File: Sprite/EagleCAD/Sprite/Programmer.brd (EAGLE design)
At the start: 49.5 x 49.5 mm, 5 parts

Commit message: Programmer Board
Finished programmer shield board
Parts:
- added JP5: (no value), SparkFun:1X03_LOCK
- moved JP3 10.2 mm to (3.81, 45.1), turned to 270 degrees
- moved JP2 5.68 mm to (32.0, 37.6), turned to 0 degrees
- moved JP1 2.57 mm to (37.1, 40.2)
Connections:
- new net 3.3V: JP2.1, JP3.1
- new net RST: JP2.2, JP3.3
- new net RXD: JP2.3, JP4.1
- new net TEST: JP1.2, JP3.2
- new net TXD: JP1.1, JP3.4
- net GND: now also JP1.3, JP5.1, JP5.2
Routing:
- net TXD: track 0.00 -> 55.0 mm
- net RST: track 0.00 -> 47.3 mm
- net TEST: track 0.00 -> 43.6 mm
- net 3.3V: track 0.00 -> 34.2 mm
- net RXD: track 0.00 -> 33.1 mm
- net GND: track 0.00 -> 16.3 mm
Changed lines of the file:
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@@
 <elements>
 <element name="U$1" library="TI_launchpad" package="LAUNCHPAD-50MM" value="LAUNCHPAD-50MM" x="0" y="-0.635"/>
-<element name="JP1" library="SparkFun" package="1X03_LOCK" value="" x="37.1" y="37.6" rot="R180"/>
-<element name="JP2" library="SparkFun" package="1X03_LOCK" value="" x="37.1" y="40.14" rot="R180"/>
-<element name="JP3" library="SparkFun" package="1X05_LOCK" value="" x="3.81" y="34.925" rot="R90"/>
+<element name="JP1" library="SparkFun" package="1X03_LOCK" value="" x="37.1" y="40.1654" rot="R180"/>
+<element name="JP2" library="SparkFun" package="1X03_LOCK" value="" x="32.0134" y="37.6094"/>
+<element name="JP3" library="SparkFun" package="1X05_LOCK" value="" x="3.81" y="45.085" rot="R270"/>
 <element name="JP4" library="SparkFun" package="1X05_LOCK" value="" x="6.35" y="34.925" rot="R90"/>
+<element name="JP5" library="SparkFun" package="1X03_LOCK" value="" x="41.91" y="47.625"/>
 </elements>
 <signals>
@@
 <signal name="GND">
 <contactref element="U$1" pad="GND"/>
+<contactref element="JP1" pad="3"/>
+<wire x1="40.5638" y1="47.752" x2="37.0332" y2="44.2214" width="0.4064" layer="16"/>
+<wire x1="37.0332" y1="44.2214" x2="33.0708" y2="44.2214" width="0.4064" layer="16"/>
+<wire x1="33.0708" y1="44.2214" x2="32.004" y2="43.1546" width="0.4064" layer="16"/>
+<wire x1="32.004" y1="43.1546" x2="32.004" y2="40.0544" width="0.4064" layer="16"/>
+<wire x1="32.004" y1="40.0544" x2="32.02" y2="40.0384" width="0.4064" layer="16"/>
+<contactref element="JP5" pad="2"/>
+<contactref element="JP5" pad="1"/>
+<wire x1="44.45" y1="47.498" x2="42.0878" y2="47.498" width="0.4064" layer="16"/>
+<wire x1="42.0878" y1="47.498" x2="41.8338" y2="47.752" width="0.4064" layer="16"/>
+<wire x1="41.8338" y1="47.752" x2="41.91" y2="47.752" width="0" layer="19" extent="16-16"/>
+<wire x1="40.5638" y1="47.752" x2="41.8338" y2="47.752" width="0" layer="19" extent="16-16"/>
+<wire x1="13.97" y1="47.625" x2="32.004" y2="43.1546" width="0" layer="19" extent="16-16"/>
+</signal>
+<signal name="3.3V">
+<contactref element="JP2" pad="1"/>
+<wire x1="32.004" y1="37.727" x2="32.0134" y2="37.7364" width="0.4064" layer="16"/>
+<contactref element="JP3" pad="1"/>
+<wire x1="32.004" y1="37.727" x2="19.8548" y2="37.727" width="0.4064" layer="16"/>
+<wire x1="19.8548" y1="37.727" x2="10.0584" y2="47.5234" width="0.4064" layer="16"/>
+<wire x1="10.0584" y1="47.5234" x2="4.6228" y2="47.5234" width="0.4064" layer="16"/>
+<wire x1="4.6228" y1="47.5234" x2="3.9116" y2="46.8122" width="0.4064" layer="16"/>
+<wire x1="3.9116" y1="46.8122" x2="3.9116" y2="45.1104" width="0.4064" layer="16"/>
+<wire x1="3.9116" y1="45.1104" x2="3.937" y2="45.085" width="0.4064" layer="16"/>
+</signal>
+<signal name="RST">
+<contactref element="JP2" pad="2"/>
+<contactref element="JP3" pad="3"/>
+<wire x1="34.5534" y1="37.4824" x2="34.5534" y2="34.147" width="0.4064" layer="1"/>
+<wire x1="34.5534" y1="34.147" x2="32.131" y2="31.7246" width="0.4064" layer="1"/>
+<wire x1="32.131" y1="31.7246" x2="3.1242" y2="31.7246" width="0.4064" layer="1"/>
+<wire x1="3.1242" y1="31.7246" x2="1.2446" y2="33.6042" width="0.4064" layer="1"/>
+<wire x1="1.2446" y1="33.6042" x2="1.2446" y2="39.5478" width="0.4064" layer="1"/>
+<wire x1="1.2446" y1="39.5478" x2="1.7272" y2="40.0304" width="0.4064" layer="1"/>
+<wire x1="1.7272" y1="40.0304" x2="3.9116" y2="40.0304" width="0.4064" layer="1"/>
+<wire x1="3.9116" y1="40.0304" x2="3.937" y2="40.005" width="0.4064" layer="1"/>
+</signal>
+<signal name="TEST">
+<contactref element="JP1" pad="2"/>
+<contactref element="JP3" pad="2"/>
+<wire x1="34.56" y1="40.2924" x2="34.56" y2="41.4114" width="0.4064" layer="1"/>
+<wire x1="34.56" y1="41.4114" x2="31.75" y2="44.2214" width="0.4064" layer="1"/>
+<wire x1="31.75" y1="44.2214" x2="11.8364" y2="44.2214" width="0.4064" layer="1"/>
+<wire x1="11.8364" y1="44.2214" x2="8.2296" y2="47.8282" width="0.4064" layer="1"/>
+<wire x1="8.2296" y1="47.8282" x2="2.4384" y2="47.8282" width="0.4064" layer="1"/>
+<wire x1="2.4384" y1="47.8282" x2="1.397" y2="46.7868" width="0.4064" layer="1"/>
+<wire x1="1.397" y1="46.7868" x2="1.397" y2="43.1292" width="0.4064" layer="1"/>
+<wire x1="1.397" y1="43.1292" x2="1.9304" y2="42.5958" width="0.4064" layer="1"/>
+<wire x1="1.9304" y1="42.5958" x2="3.6322" y2="42.5958" width="0.4064" layer="1"/>
+<wire x1="3.6322" y1="42.5958" x2="3.683" y2="42.545" width="0.4064" layer="1"/>
+</signal>
+<signal name="TXD">
+<contactref element="JP3" pad="4"/>
+<contactref element="JP1" pad="1"/>
+<wire x1="37.1" y1="40.0384" x2="39.1334" y2="40.0384" width="0.4064" layer="16"/>
+<wire x1="39.1334" y1="40.0384" x2="40.4114" y2="38.7604" width="0.4064" layer="16"/>
+<wire x1="40.4114" y1="38.7604" x2="40.4114" y2="32.9946" width="0.4064" layer="16"/>
+<wire x1="40.4114" y1="32.9946" x2="39.7764" y2="32.3596" width="0.4064" layer="16"/>
+<wire x1="39.7764" y1="32.3596" x2="2.8194" y2="32.3596" width="0.4064" layer="16"/>
+<wire x1="2.8194" y1="32.3596" x2="1.4478" y2="33.7312" width="0.4064" layer="16"/>
+<wire x1="1.4478" y1="33.7312" x2="1.4478" y2="36.83" width="0.4064" layer="16"/>
+<wire x1="1.4478" y1="36.83" x2="2.0574" y2="37.4396" width="0.4064" layer="16"/>
+<wire x1="2.0574" y1="37.4396" x2="3.6576" y2="37.4396" width="0.4064" layer="16"/>
+<wire x1="3.6576" y1="37.4396" x2="3.683" y2="37.465" width="0.4064" layer="16"/>
+</signal>
+<signal name="RXD">
+<contactref element="JP4" pad="1"/>
+<contactref element="JP2" pad="3"/>
+<wire x1="37.0934" y1="37.7364" x2="37.0934" y2="35.925" width="0.4064" layer="16"/>
+<wire x1="37.0934" y1="35.925" x2="36.068" y2="34.8996" width="0.4064" layer="16"/>
+<wire x1="36.068" y1="34.8996" x2="6.2484" y2="34.8996" width="0.4064" layer="16"/>
+<wire x1="6.2484" y1="34.8996" x2="6.223" y2="34.925" width="0.4064" layer="16"/>
 </signal>
 </signals>

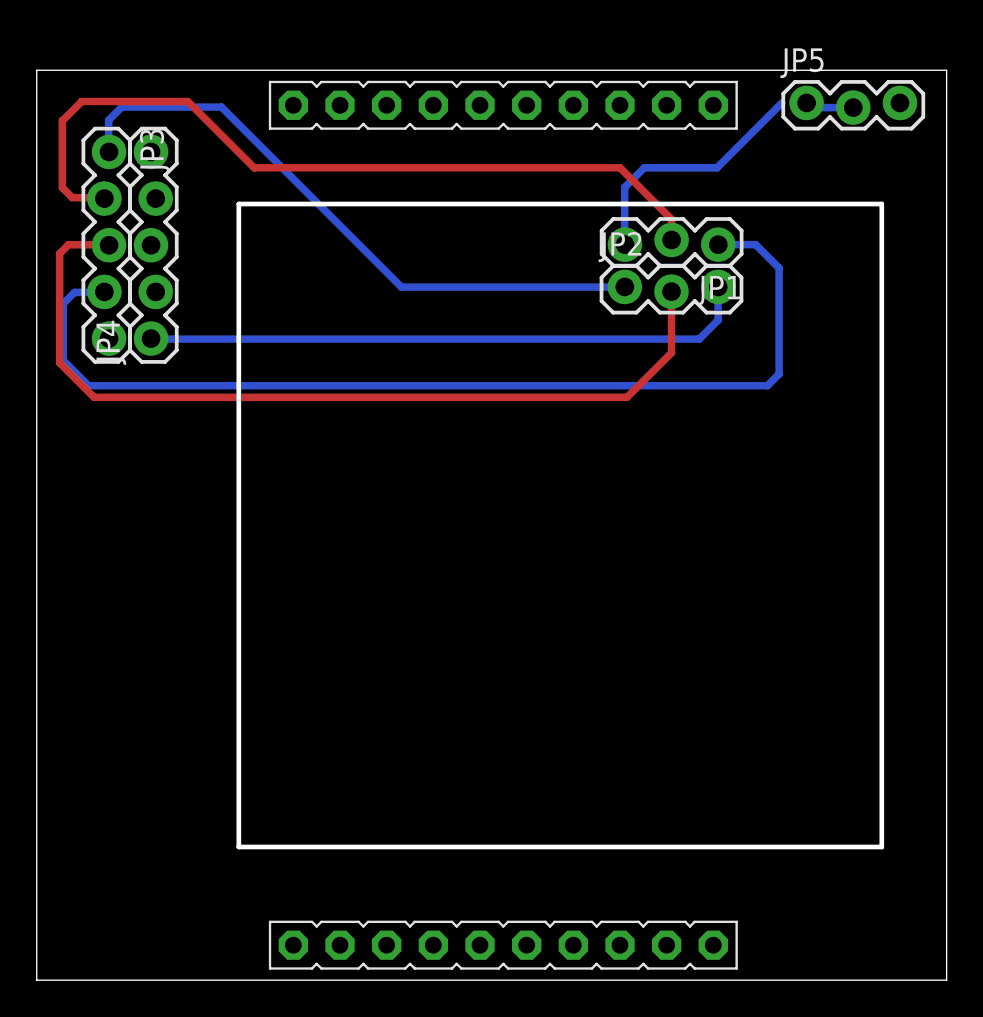
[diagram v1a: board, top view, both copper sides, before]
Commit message: Finished Programmer Board
Added KickSat Silkscreen
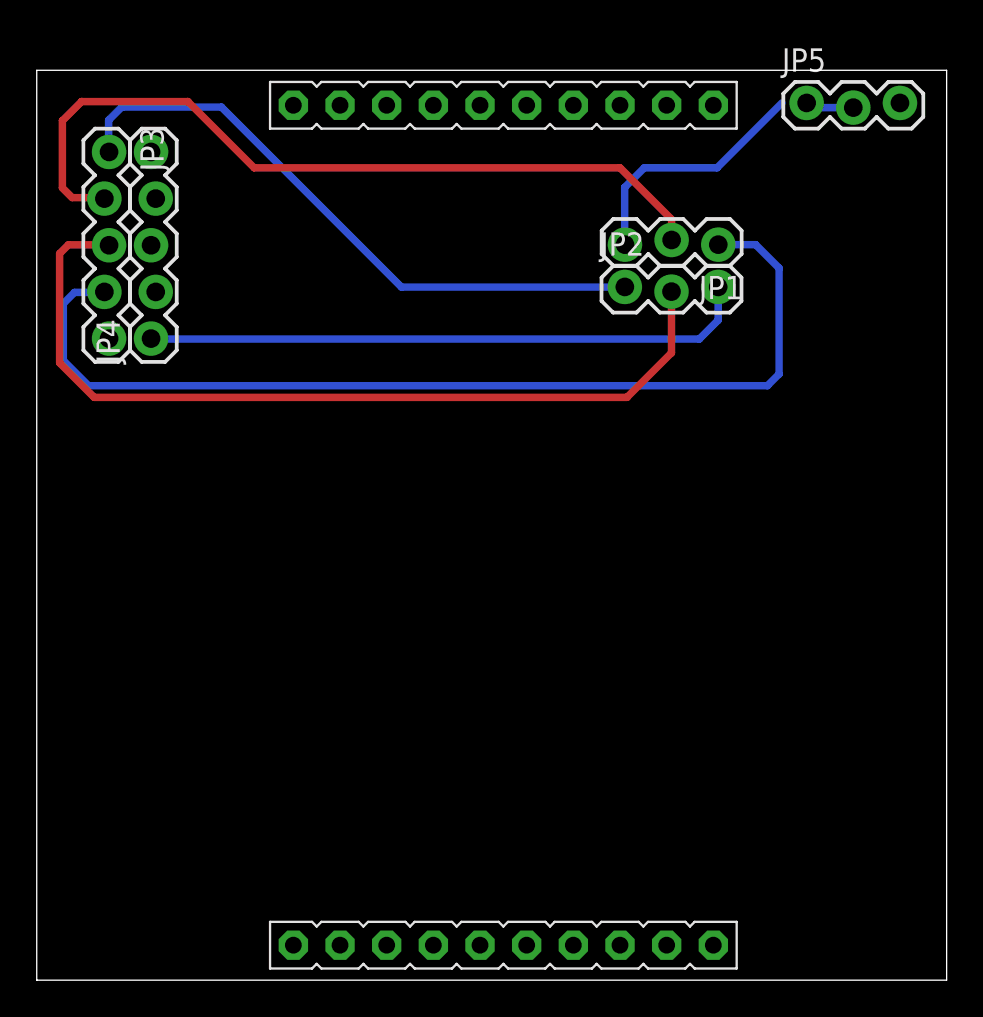
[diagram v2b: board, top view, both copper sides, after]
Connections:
- net RXD: now also JP1.1, JP3.4; no longer JP2.3, JP4.1
- net TXD: now also JP2.3, JP4.1; no longer JP1.1, JP3.4
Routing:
- net TXD: track 55.0 -> 33.1 mm
- net RXD: track 33.1 -> 55.0 mm
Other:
- board text added: "/Users/zacman/Documents/Graphics/KickSat/kicksatlogo4-silkscreen.bmp"
